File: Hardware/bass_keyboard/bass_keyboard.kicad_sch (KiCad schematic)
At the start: 165 parts

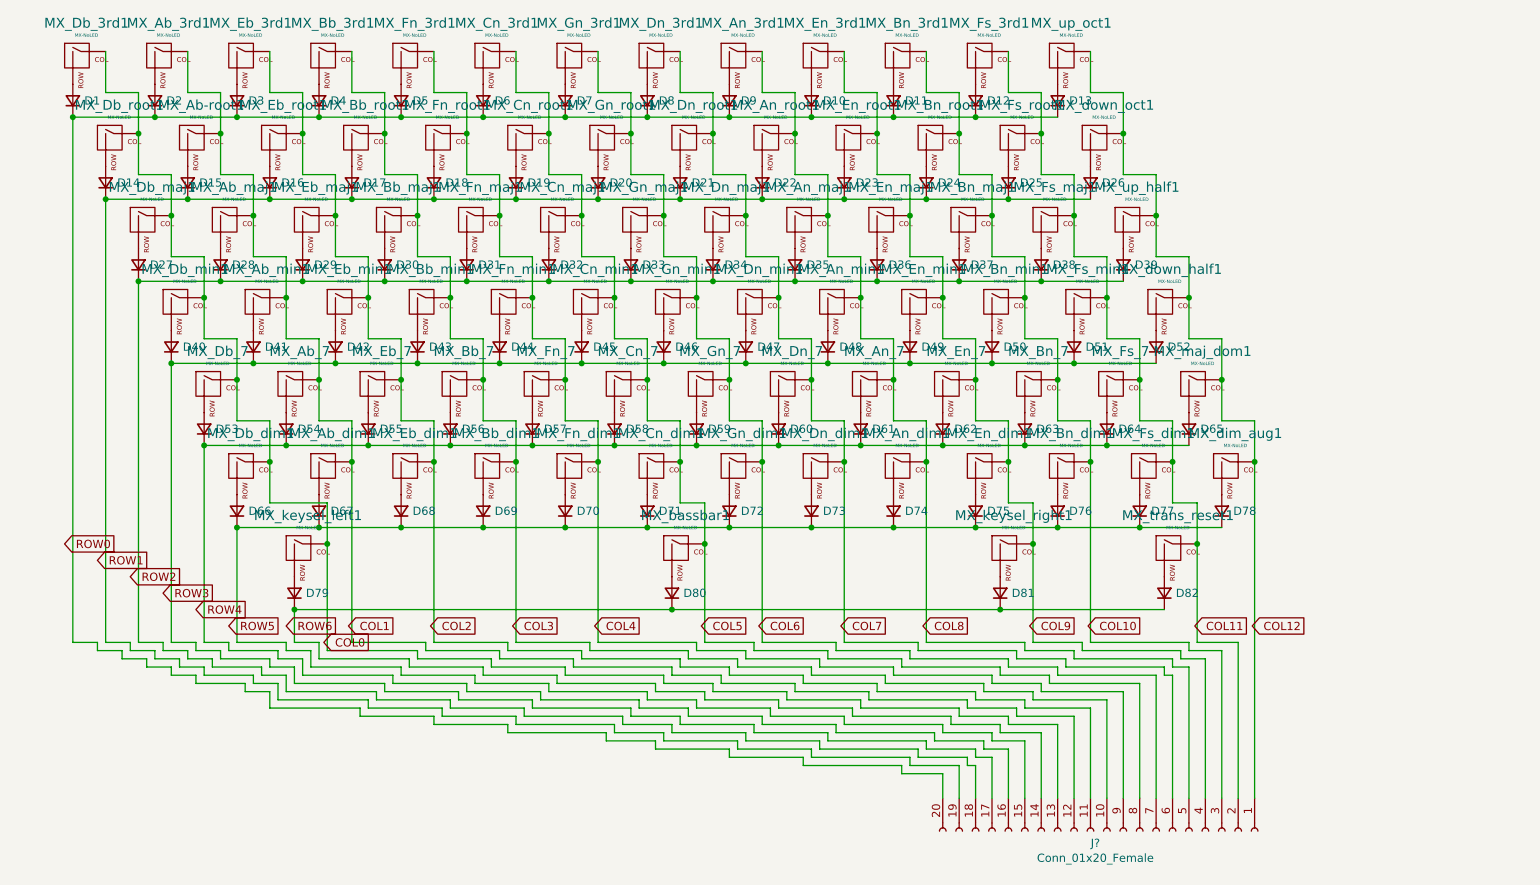
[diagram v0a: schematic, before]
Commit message: Future-proof bass keyboard
Filled out the rest of the lower function row for futureproofing and expandability. Settled on a  2x16 pin header connector. Added indicator LEDs for the right side toggles, and speaker which is to be routed through the same cable as the keyboard.
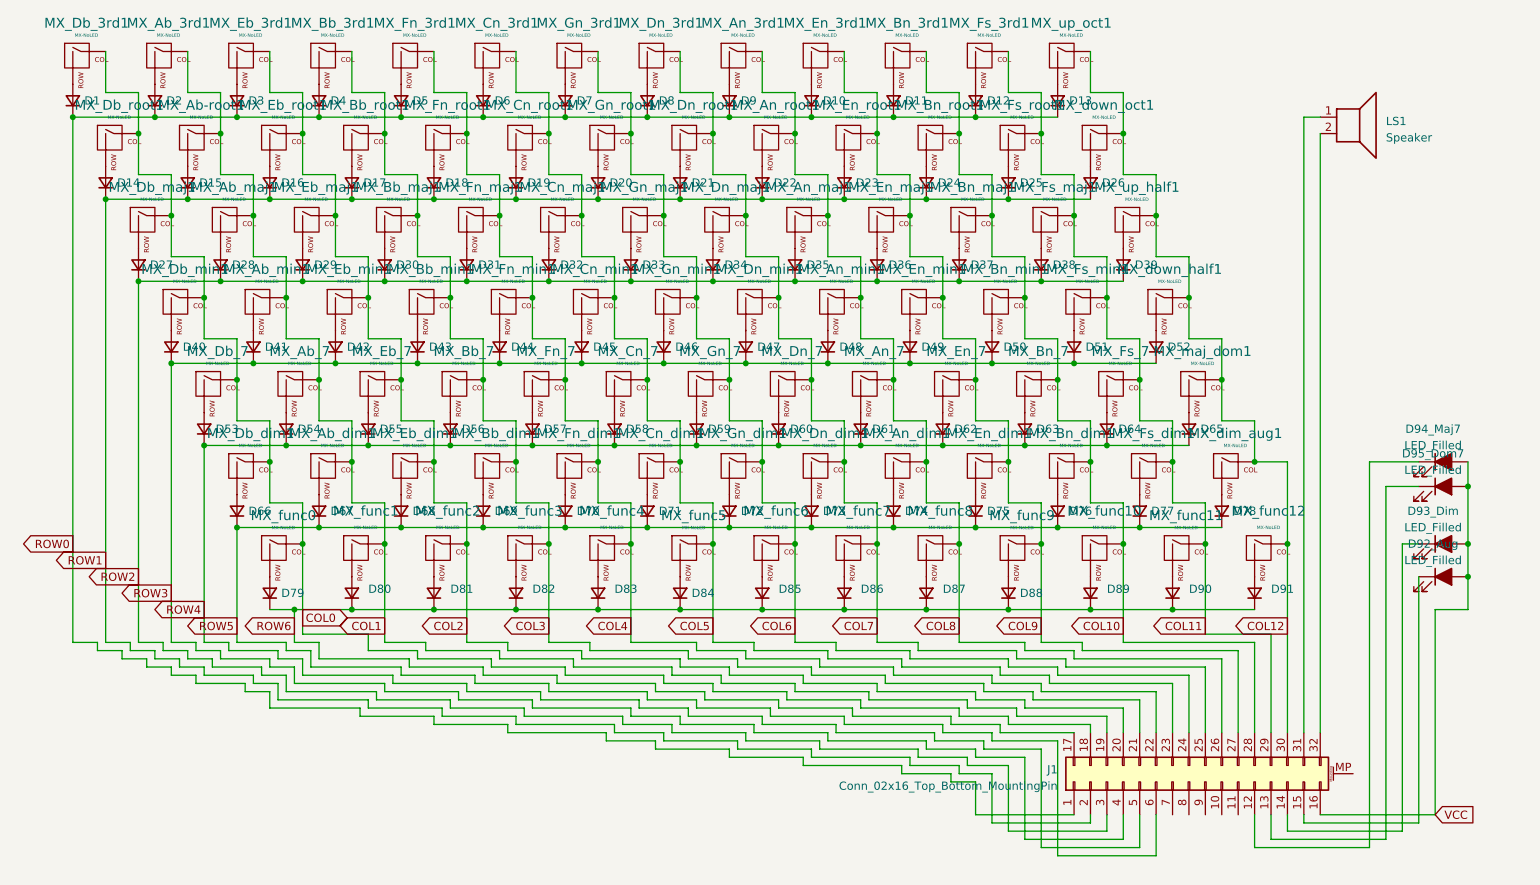
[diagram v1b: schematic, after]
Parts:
- removed J?: Conn_01x20_Female, symbol Connector:Conn_01x20_Female
- added D80, D81, D83, D85, D86, D87, D89, D90, D91: D_Small, symbol Device:D_Small
- added D92_Aug, D93_Dim, D94_Maj7, D95_Dom7: LED_Filled, random-keyboard-parts:LED_D3.0mm-Pretty, symbol Device:LED_Filled
- added J1: Conn_02x16_Top_Bottom_MountingPin, symbol Connector_Generic_MountingPin:Conn_02x16_Top_Bottom_MountingPin
- added LS1: Speaker, symbol Device:Speaker
- added MX_func1, MX_func10, MX_func12, MX_func2, MX_func3, MX_func4, MX_func6, MX_func7, MX_func8: MX-NoLED, symbol MX_Alps_Hybrid:MX-NoLED
- D82: footprint Diode_SMD:D_SOD-123 -> (none)
- renumbered D80 to D84, D81 to D88, MX_keysel_left1 to MX_func0, MX_trans_reset1 to MX_func11, MX_bassbar1 to MX_func5, MX_keysel_right1 to MX_func9
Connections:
- net COL0: now also MX_Db_3rd1.1 (COL), MX_Db_7.1 (COL), MX_Db_dim1.1 (COL), MX_Db_maj1.1 (COL), MX_Db_min1.1 (COL), MX_Db_root1.1 (COL), MX_func0.1 (COL), J1.18 (Pin_18); no longer MX_Ab-root1.1 (COL), MX_Ab_3rd1.1 (COL), MX_Ab_7.1 (COL), MX_Ab_dim1.1 (COL), MX_Ab_maj1.1 (COL), MX_Ab_min1.1 (COL)
- net COL1: now also MX_Ab-root1.1 (COL), MX_Ab_3rd1.1 (COL), MX_Ab_7.1 (COL), MX_Ab_dim1.1 (COL), MX_Ab_maj1.1 (COL), MX_Ab_min1.1 (COL), J1.19 (Pin_19), MX_func1.1 (COL)
- net COL10: now also MX_Bn_3rd1.1 (COL), MX_Bn_7.1 (COL), MX_Bn_dim1.1 (COL), MX_Bn_maj1.1 (COL), MX_Bn_min1.1 (COL), MX_Bn_root1.1 (COL), J1.28 (Pin_28), MX_func10.1 (COL)
- net COL11: now also MX_Fs_3rd1.1 (COL), MX_Fs_7.1 (COL), MX_Fs_dim1.1 (COL), MX_Fs_maj1.1 (COL), MX_Fs_min1.1 (COL), MX_Fs_root1.1 (COL), MX_func11.1 (COL), J1.29 (Pin_29)
- net COL12: now also MX_dim_aug1.1 (COL), MX_down_half1.1 (COL), MX_down_oct1.1 (COL), MX_maj_dom1.1 (COL), MX_up_half1.1 (COL), MX_up_oct1.1 (COL), J1.30 (Pin_30), MX_func12.1 (COL)
- net COL2: now also MX_Eb_3rd1.1 (COL), MX_Eb_7.1 (COL), MX_Eb_dim1.1 (COL), MX_Eb_maj1.1 (COL), MX_Eb_min1.1 (COL), MX_Eb_root1.1 (COL), J1.20 (Pin_20), MX_func2.1 (COL)
- net COL3: now also MX_Bb_3rd1.1 (COL), MX_Bb_7.1 (COL), MX_Bb_dim1.1 (COL), MX_Bb_maj1.1 (COL), MX_Bb_min1.1 (COL), MX_Bb_root1.1 (COL), J1.21 (Pin_21), MX_func3.1 (COL)
- net COL4: now also MX_Fn_3rd1.1 (COL), MX_Fn_7.1 (COL), MX_Fn_dim1.1 (COL), MX_Fn_maj1.1 (COL), MX_Fn_min1.1 (COL), MX_Fn_root1.1 (COL), J1.22 (Pin_22), MX_func4.1 (COL)
- net COL5: now also MX_Cn_3rd1.1 (COL), MX_Cn_7.1 (COL), MX_Cn_dim1.1 (COL), MX_Cn_maj1.1 (COL), MX_Cn_min1.1 (COL), MX_Cn_root1.1 (COL), MX_func5.1 (COL), J1.23 (Pin_23)
- net COL6: now also MX_Gn_3rd1.1 (COL), MX_Gn_7.1 (COL), MX_Gn_dim1.1 (COL), MX_Gn_maj1.1 (COL), MX_Gn_min1.1 (COL), MX_Gn_root1.1 (COL), J1.24 (Pin_24), MX_func6.1 (COL)
- net COL7: now also MX_Dn_3rd1.1 (COL), MX_Dn_7.1 (COL), MX_Dn_dim1.1 (COL), MX_Dn_maj1.1 (COL), MX_Dn_min1.1 (COL), MX_Dn_root1.1 (COL), J1.25 (Pin_25), MX_func7.1 (COL)
- net COL8: now also MX_An_3rd1.1 (COL), MX_An_7.1 (COL), MX_An_dim1.1 (COL), MX_An_maj1.1 (COL), MX_An_min1.1 (COL), MX_An_root1.1 (COL), J1.26 (Pin_26), MX_func8.1 (COL)
- net COL9: now also MX_En_3rd1.1 (COL), MX_En_7.1 (COL), MX_En_dim1.1 (COL), MX_En_maj1.1 (COL), MX_En_min1.1 (COL), MX_En_root1.1 (COL), MX_func9.1 (COL), J1.27 (Pin_27)
- net ROW0: now also D1.1 (K), D10.1 (K), D11.1 (K), D12.1 (K), D13.1 (K), D2.1 (K), D3.1 (K), D4.1 (K), D5.1 (K), D6.1 (K), D7.1 (K), D8.1 (K), D9.1 (K), J1.1 (Pin_1)
- net ROW1: now also D14.1 (K), D15.1 (K), D16.1 (K), D17.1 (K), D18.1 (K), D19.1 (K), D20.1 (K), D21.1 (K), D22.1 (K), D23.1 (K), D24.1 (K), D25.1 (K), D26.1 (K), J1.2 (Pin_2)
- net ROW2: now also D27.1 (K), D28.1 (K), D29.1 (K), D30.1 (K), D31.1 (K), D32.1 (K), D33.1 (K), D34.1 (K), D35.1 (K), D36.1 (K), D37.1 (K), D38.1 (K), D39.1 (K), J1.3 (Pin_3)
- net ROW3: now also D40.1 (K), D41.1 (K), D42.1 (K), D43.1 (K), D44.1 (K), D45.1 (K), D46.1 (K), D47.1 (K), D48.1 (K), D49.1 (K), D50.1 (K), D51.1 (K), D52.1 (K), J1.4 (Pin_4)
- net ROW4: now also D53.1 (K), D54.1 (K), D55.1 (K), D56.1 (K), D57.1 (K), D58.1 (K), D59.1 (K), D60.1 (K), D61.1 (K), D62.1 (K), D63.1 (K), D64.1 (K), D65.1 (K), J1.5 (Pin_5)
- net ROW5: now also D66.1 (K), D67.1 (K), D68.1 (K), D69.1 (K), D70.1 (K), D71.1 (K), D72.1 (K), D73.1 (K), D74.1 (K), D75.1 (K), D76.1 (K), D77.1 (K), D78.1 (K), J1.6 (Pin_6)
- net ROW6: now also D79.1 (K), D82.1 (K), D84.1 (K), D88.1 (K), D80.1 (K), D81.1 (K), D83.1 (K), D85.1 (K), D86.1 (K), D87.1 (K), D89.1 (K), D90.1 (K), D91.1 (K), J1.17 (Pin_17)
- net at MX_func11.2 (ROW): now also D90.2 (A); no longer D82.2 (A)
- new net: D83.2 (A), MX_func4.2 (ROW)
- new net: D81.2 (A), MX_func2.2 (ROW)
- new net: D86.2 (A), MX_func7.2 (ROW)
- new net: D89.2 (A), MX_func10.2 (ROW)
- new net: D94_Maj7.1 (K), J1.12 (Pin_12)
- new net: D95_Dom7.1 (K), J1.13 (Pin_13)
- new net: D93_Dim.1 (K), J1.14 (Pin_14)
- new net: D92_Aug.1 (K), J1.15 (Pin_15)
- new net: J1.31 (Pin_31), LS1.1
- new net: J1.32 (Pin_32), LS1.2
- new net: D80.2 (A), MX_func1.2 (ROW)
- new net: D82.2 (A), MX_func3.2 (ROW)
- new net: D85.2 (A), MX_func6.2 (ROW)
- new net: D91.2 (A), MX_func12.2 (ROW)
- new net: D87.2 (A), MX_func8.2 (ROW)
- new net VCC: D92_Aug.2 (A), D93_Dim.2 (A), D94_Maj7.2 (A), D95_Dom7.2 (A), J1.16 (Pin_16)
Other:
- title: (none) -> Synharmonium Bass Keyboard PCB
- moved on the sheet: D79, D84, D88, MX_func0, MX_func11, MX_func5, MX_func9

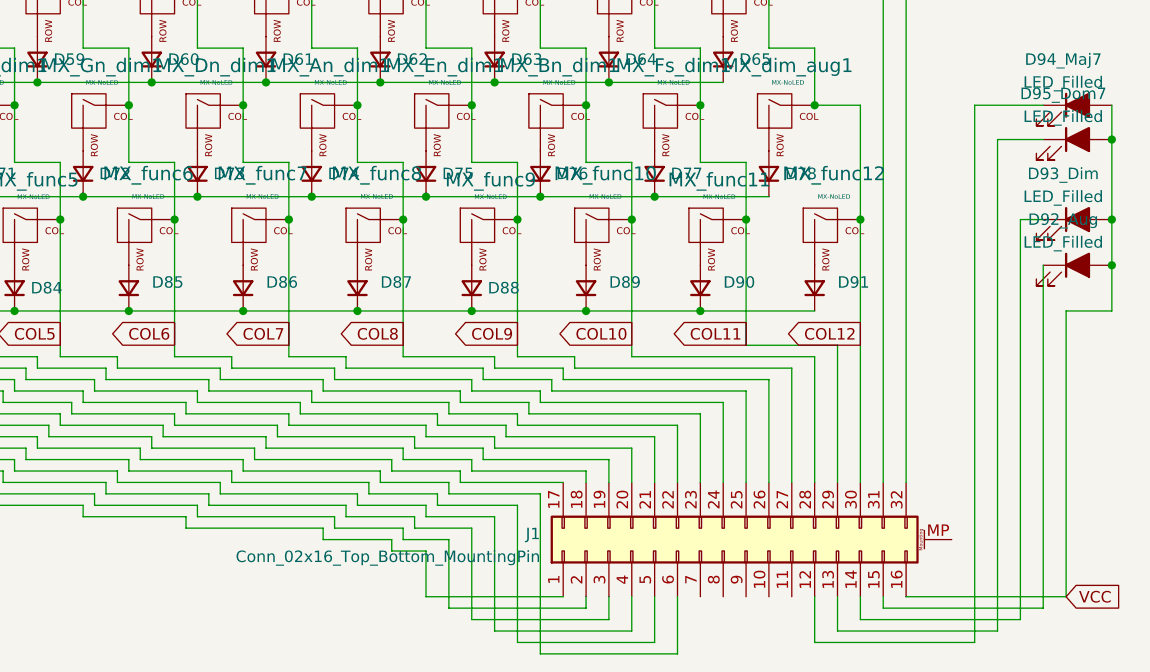
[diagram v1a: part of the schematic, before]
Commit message: Begin Bass Keyboard PCB design
Started placing switch footprints for the root row.
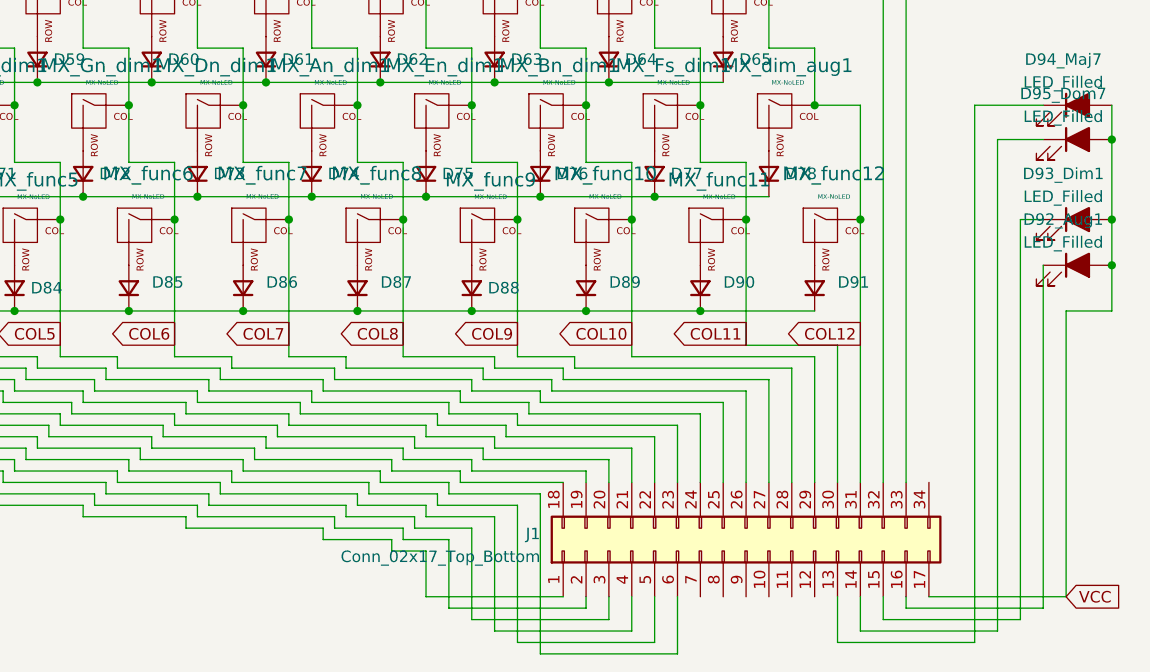
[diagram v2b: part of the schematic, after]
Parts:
- removed J1: Conn_02x16_Top_Bottom_MountingPin, symbol Connector_Generic_MountingPin:Conn_02x16_Top_Bottom_MountingPin
- added J1: Conn_02x17_Top_Bottom, symbol Connector_Generic:Conn_02x17_Top_Bottom
- D80, D81, D82, D83, D85, D86, D87, D89, D90, D91: footprint (none) -> Diode_SMD:D_SOD-123
- MX_Ab-root1, MX_Ab_3rd1, MX_Ab_7, MX_Ab_dim1, MX_Ab_maj1, MX_Ab_min1, MX_An_3rd1, MX_An_7, MX_An_dim1, MX_An_maj1, MX_An_min1, MX_An_root1, MX_Bb_3rd1, MX_Bb_7, MX_Bb_dim1, MX_Bb_maj1, MX_Bb_min1, MX_Bb_root1, MX_Bn_3rd1, MX_Bn_7, MX_Bn_dim1, MX_Bn_maj1, MX_Bn_min1, MX_Bn_root1, MX_Cn_3rd1, MX_Cn_7, MX_Cn_dim1, MX_Cn_maj1, MX_Cn_min1, MX_Cn_root1, MX_Db_3rd1, MX_Db_7, MX_Db_dim1, MX_Db_maj1, MX_Db_min1, MX_Db_root1, MX_Dn_3rd1, MX_Dn_7, MX_Dn_dim1, MX_Dn_maj1, MX_Dn_min1, MX_Dn_root1, MX_Eb_3rd1, MX_Eb_7, MX_Eb_dim1, MX_Eb_maj1, MX_Eb_min1, MX_Eb_root1, MX_En_3rd1, MX_En_7, MX_En_dim1, MX_En_maj1, MX_En_min1, MX_En_root1, MX_Fn_3rd1, MX_Fn_7, MX_Fn_dim1, MX_Fn_maj1, MX_Fn_min1, MX_Fn_root1, MX_Fs_3rd1, MX_Fs_7, MX_Fs_dim1, MX_Fs_maj1, MX_Fs_min1, MX_Fs_root1, MX_Gn_3rd1, MX_Gn_7, MX_Gn_dim1, MX_Gn_maj1, MX_Gn_min1, MX_Gn_root1, MX_dim_aug1, MX_down_half1, MX_down_oct1, MX_func0, MX_func1, MX_func10, MX_func11, MX_func12, MX_func2, MX_func3, MX_func4, MX_func5, MX_func6, MX_func7, MX_func8, MX_func9, MX_maj_dom1, MX_up_half1, MX_up_oct1: footprint (none) -> Button_Switch_Keyboard:SW_Cherry_MX_1.00u_PCB
- renumbered D92_Aug to D92_Aug1, D93_Dim to D93_Dim1
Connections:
- net COL0: now also J1.19 (Pin_19)
- net COL1: now also J1.20 (Pin_20)
- net COL10: now also J1.29 (Pin_29)
- net COL11: now also J1.30 (Pin_30)
- net COL12: now also J1.31 (Pin_31)
- net COL2: now also J1.21 (Pin_21)
- net COL3: now also J1.22 (Pin_22)
- net COL4: now also J1.23 (Pin_23)
- net COL5: now also J1.24 (Pin_24)
- net COL6: now also J1.25 (Pin_25)
- net COL7: now also J1.26 (Pin_26)
- net COL8: now also J1.27 (Pin_27)
- net COL9: now also J1.28 (Pin_28)
- net ROW0: now also J1.1 (Pin_1)
- net ROW1: now also J1.2 (Pin_2)
- net ROW2: now also J1.3 (Pin_3)
- net ROW3: now also J1.4 (Pin_4)
- net ROW4: now also J1.5 (Pin_5)
- net ROW5: now also J1.6 (Pin_6)
- net ROW6: now also J1.18 (Pin_18)
- net VCC: now also J1.17 (Pin_17)
- net at D94_Maj7.1 (K): now also J1.13 (Pin_13)
- net at D95_Dom7.1 (K): now also J1.14 (Pin_14)
- net at D93_Dim1.1 (K): now also J1.15 (Pin_15)
- net at D92_Aug1.1 (K): now also J1.16 (Pin_16)
- net at LS1.1: now also J1.32 (Pin_32)
- net at LS1.2: now also J1.33 (Pin_33)

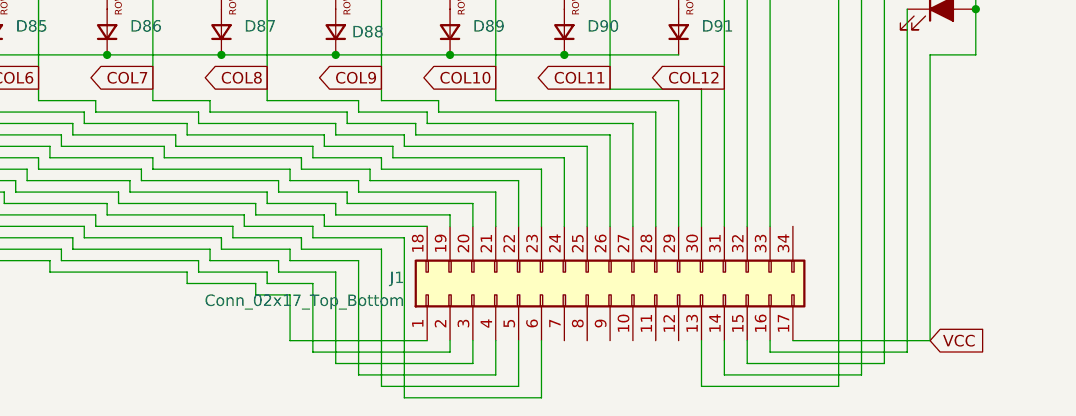
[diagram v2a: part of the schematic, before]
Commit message: Finishing layout, routing
Got all of the footprints where they need to be, created the pcb outline, and used Freerouting to route connections, doing some final connections by hand.
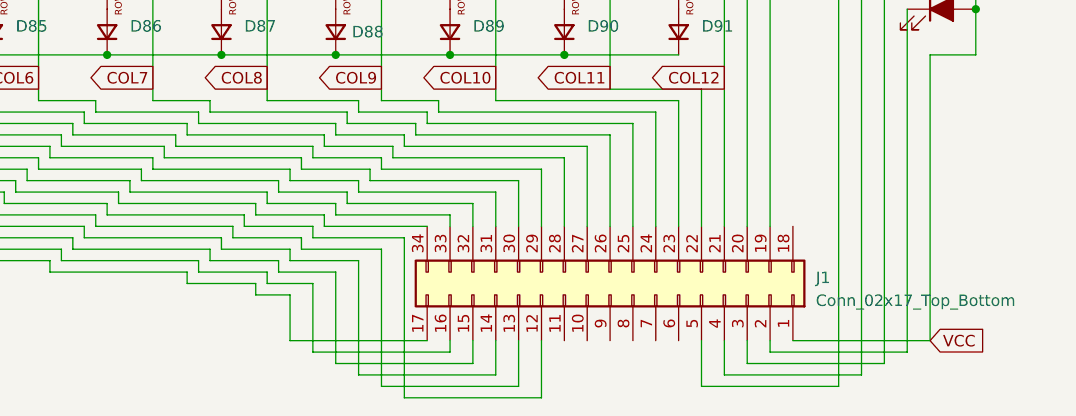
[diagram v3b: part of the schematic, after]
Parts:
- J1: footprint (none) -> Connector_IDC:IDC-Header_2x17_P2.54mm_Vertical
- LS1: footprint (none) -> Connector_Wire:SolderWire-2sqmm_1x02_P7.8mm_D2mm_OD3.9mm
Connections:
- net COL0: now also J1.33 (Pin_33); no longer J1.19 (Pin_19)
- net COL1: now also J1.32 (Pin_32); no longer J1.20 (Pin_20)
- net COL10: now also J1.23 (Pin_23); no longer J1.29 (Pin_29)
- net COL11: now also J1.22 (Pin_22); no longer J1.30 (Pin_30)
- net COL12: now also J1.21 (Pin_21); no longer J1.31 (Pin_31)
- net COL2: now also J1.31 (Pin_31); no longer J1.21 (Pin_21)
- net COL3: now also J1.30 (Pin_30); no longer J1.22 (Pin_22)
- net COL4: now also J1.29 (Pin_29); no longer J1.23 (Pin_23)
- net COL5: now also J1.28 (Pin_28); no longer J1.24 (Pin_24)
- net COL6: now also J1.27 (Pin_27); no longer J1.25 (Pin_25)
- net COL8: now also J1.25 (Pin_25); no longer J1.27 (Pin_27)
- net COL9: now also J1.24 (Pin_24); no longer J1.28 (Pin_28)
- net ROW0: now also J1.17 (Pin_17); no longer J1.1 (Pin_1)
- net ROW1: now also J1.16 (Pin_16); no longer J1.2 (Pin_2)
- net ROW2: now also J1.15 (Pin_15); no longer J1.3 (Pin_3)
- net ROW3: now also J1.14 (Pin_14); no longer J1.4 (Pin_4)
- net ROW4: now also J1.13 (Pin_13); no longer J1.5 (Pin_5)
- net ROW5: now also J1.12 (Pin_12); no longer J1.6 (Pin_6)
- net ROW6: now also J1.34 (Pin_34); no longer J1.18 (Pin_18)
- net VCC: now also J1.1 (Pin_1); no longer J1.17 (Pin_17)
- net at D94_Maj7.1 (K): now also J1.5 (Pin_5); no longer J1.13 (Pin_13)
- net at D95_Dom7.1 (K): now also J1.4 (Pin_4); no longer J1.14 (Pin_14)
- net at D93_Dim1.1 (K): now also J1.3 (Pin_3); no longer J1.15 (Pin_15)
- net at D92_Aug1.1 (K): now also J1.2 (Pin_2); no longer J1.16 (Pin_16)
- net at LS1.1: now also J1.20 (Pin_20); no longer J1.32 (Pin_32)
- net at LS1.2: now also J1.19 (Pin_19); no longer J1.33 (Pin_33)
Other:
- title: Synharmonium Bass Keyboard PCB -> Synharmonium Bass Keyboard, Prototyping Master
- moved on the sheet: J1
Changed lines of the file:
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@@
   (paper "A4")
   (title_block
-    (title "Synharmonium Bass Keyboard PCB")
+    (title "Synharmonium Bass Keyboard, Prototyping Master")
     (date "2023-04-06")
     (rev "0.1")
@@
     )
   )
-  (symbol (lib_id "Connector_Generic:Conn_02x17_Top_Bottom") (at 212.09 151.13 90) (unit 1)
-    (in_bom yes) (on_board yes) (dnp no) (fields_autoplaced)
-    (property "Reference" "J1" (at 189.23 149.225 90)
+  (symbol (lib_id "Connector_Generic:Conn_02x17_Top_Bottom") (at 212.09 151.13 270) (mirror x) (unit 1)
+    (in_bom yes) (on_board yes) (dnp no)
+    (property "Reference" "J1" (at 234.95 149.225 90)
       (effects (font (size 1.27 1.27)) (justify left))
     )
-    (property "Value" "Conn_02x17_Top_Bottom" (at 189.23 151.765 90)
+    (property "Value" "Conn_02x17_Top_Bottom" (at 234.95 151.765 90)
       (effects (font (size 1.27 1.27)) (justify left))
     )
-    (property "Footprint" "" (at 212.09 151.13 0)
+    (property "Footprint" "Connector_IDC:IDC-Header_2x17_P2.54mm_Vertical" (at 212.09 151.13 0)
       (effects (font (size 1.27 1.27)) hide)
     )
@@
       (effects (font (size 1.27 1.27)) (justify left))
     )
-    (property "Footprint" "" (at 234.95 53.34 0)
+    (property "Footprint" "Connector_Wire:SolderWire-2sqmm_1x02_P7.8mm_D2mm_OD3.9mm" (at 234.95 53.34 0)
       (effects (font (size 1.27 1.27)) hide)
     )
